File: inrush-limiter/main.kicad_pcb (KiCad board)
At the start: 2 copper layers, 27 parts, among them K1 RELAY_2RT, P1 CONN_01X04, P2 CONN_01X02, Q1 PN2222A, Q2 PN2222A, U1 LM393

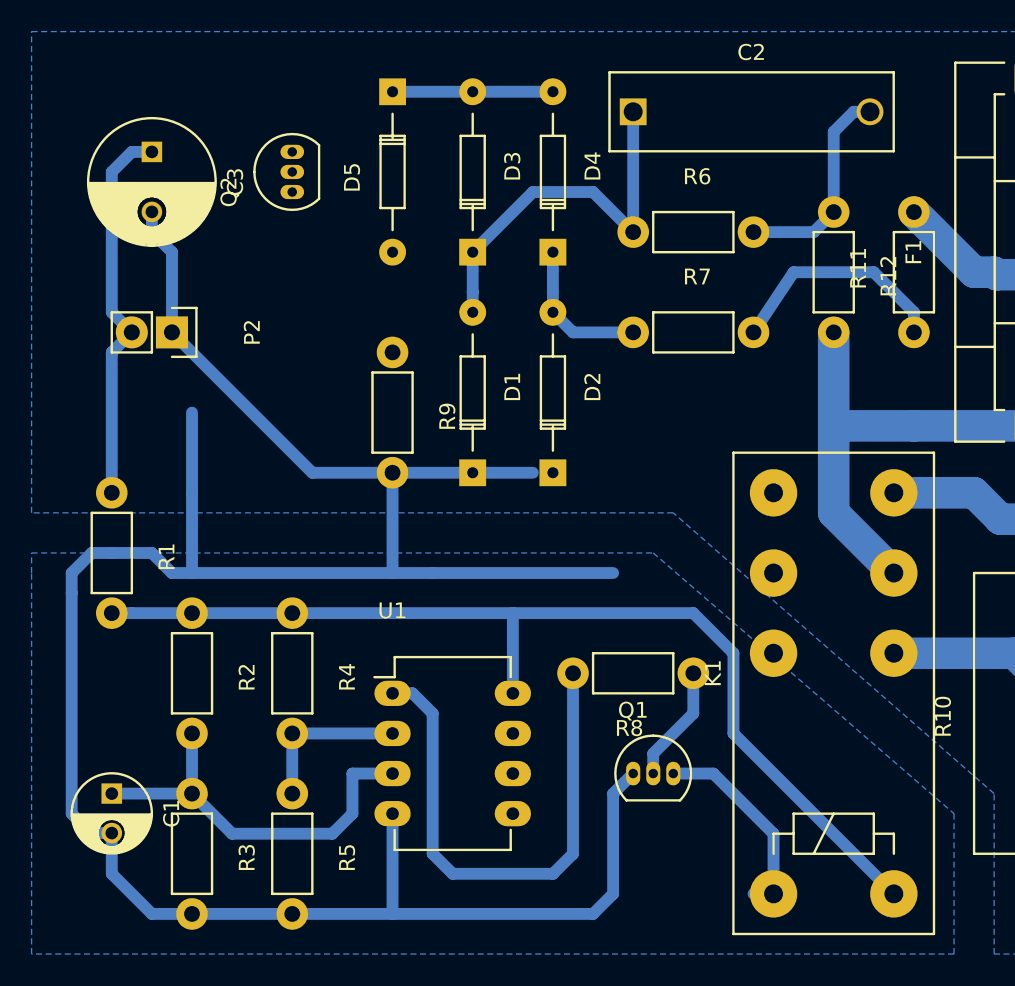
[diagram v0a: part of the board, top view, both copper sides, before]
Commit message: .25 trace and space
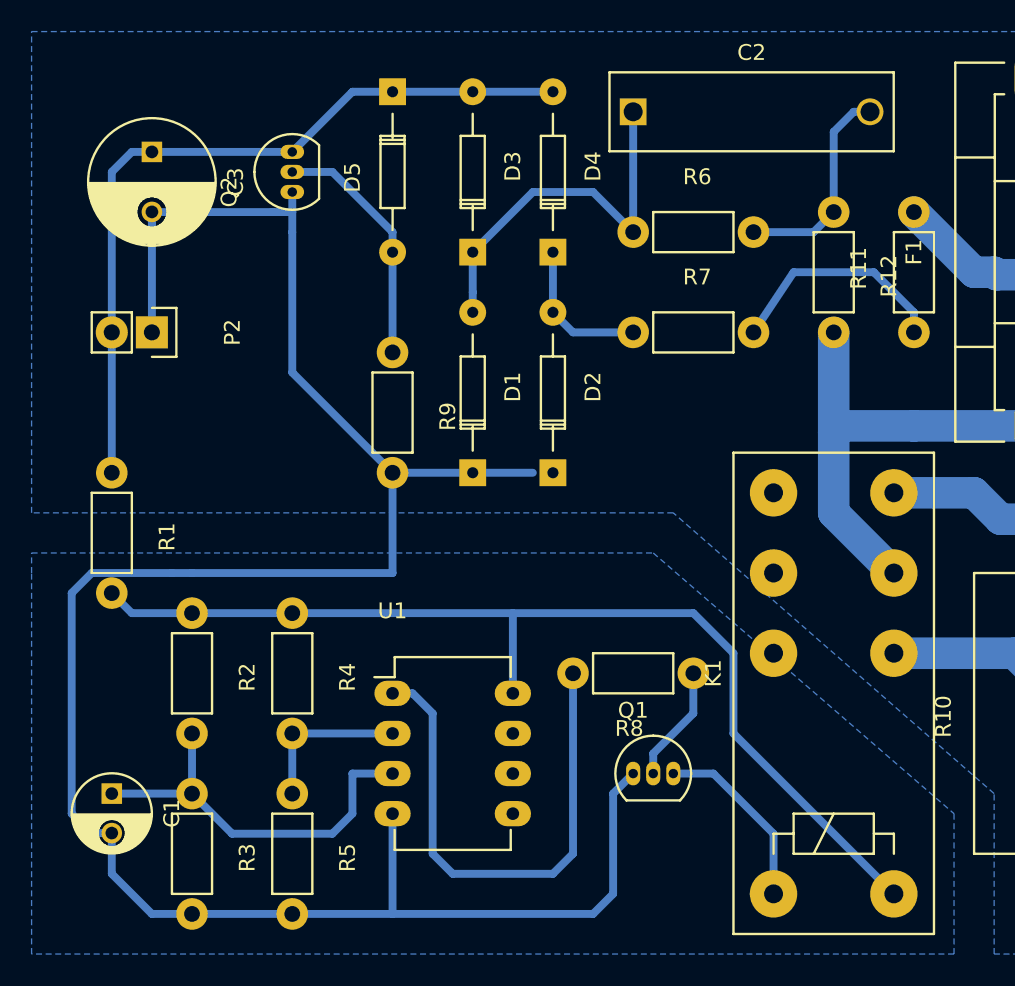
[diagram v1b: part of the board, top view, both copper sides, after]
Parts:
- moved P2 1.27 mm to (121.9, 58.4)
- moved R1 1.27 mm to (119.4, 67.3)
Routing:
- net Net-(D5-Pad2): track 0.00 -> 15.6 mm
- net +5V: track 34.6 -> 49.1 mm
- net GND: track 155.4 -> 141.9 mm
- net Net-(K1-PadA2): track 65.0 -> 65.5 mm
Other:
- net class Default: clearance 0.75 -> 0.5; trace_width 0.75 -> 0.5
- rule trace_clearance: 0.75 -> 0.5

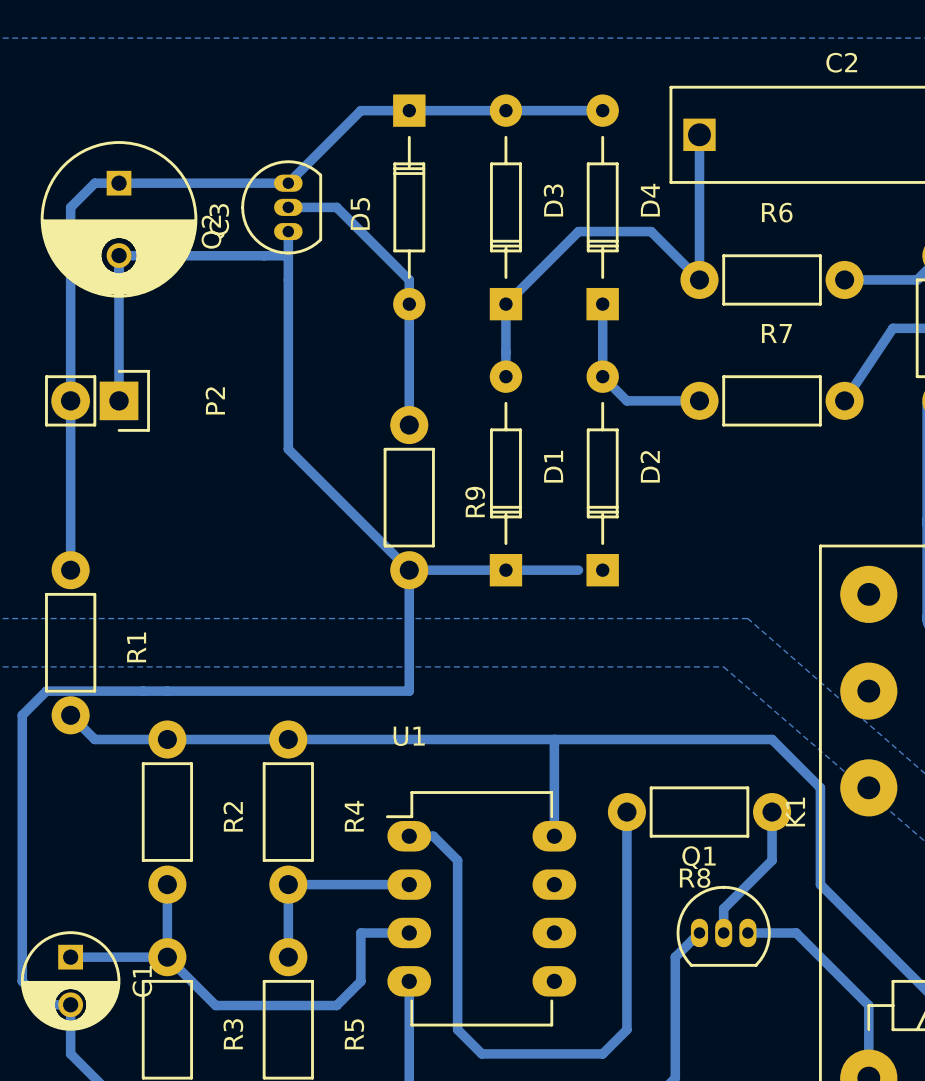
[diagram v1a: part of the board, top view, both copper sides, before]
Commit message: .5 trace and 1mm clearance
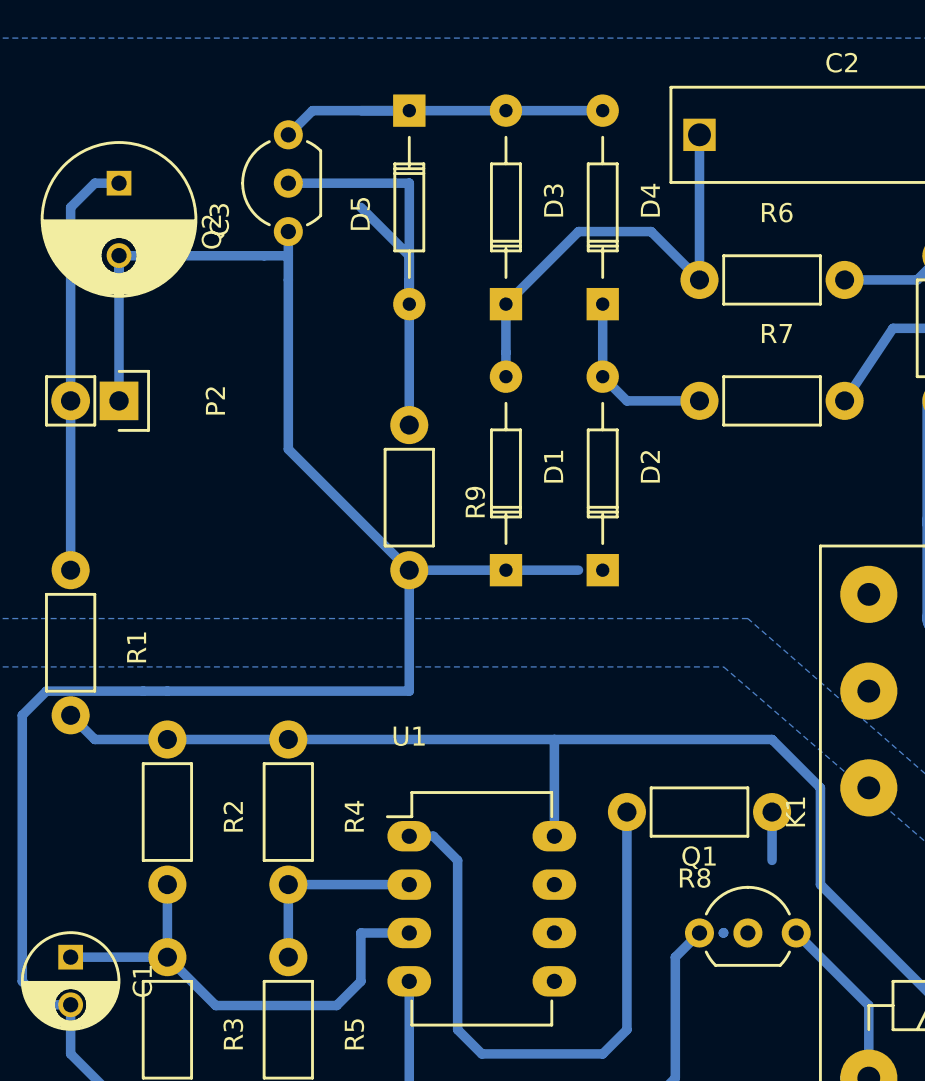
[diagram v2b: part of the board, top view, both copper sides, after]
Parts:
- Q1, Q2: footprint TO_SOT_Packages_THT:TO-92_Inline_Narrow_Oval -> TO_SOT_Packages_THT:TO-92_Inline_Wide
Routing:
- net Net-(D5-Pad2): track 15.6 -> 26.5 mm
- net +5V: track 49.1 -> 41.7 mm
- net Net-(Q1-Pad2): track 7.45 -> 2.59 mm
- net Net-(K1-PadA1): track 13.0 -> 10.5 mm
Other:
- net class Default: clearance 0.5 -> 1
- rule trace_clearance: 0.5 -> 1

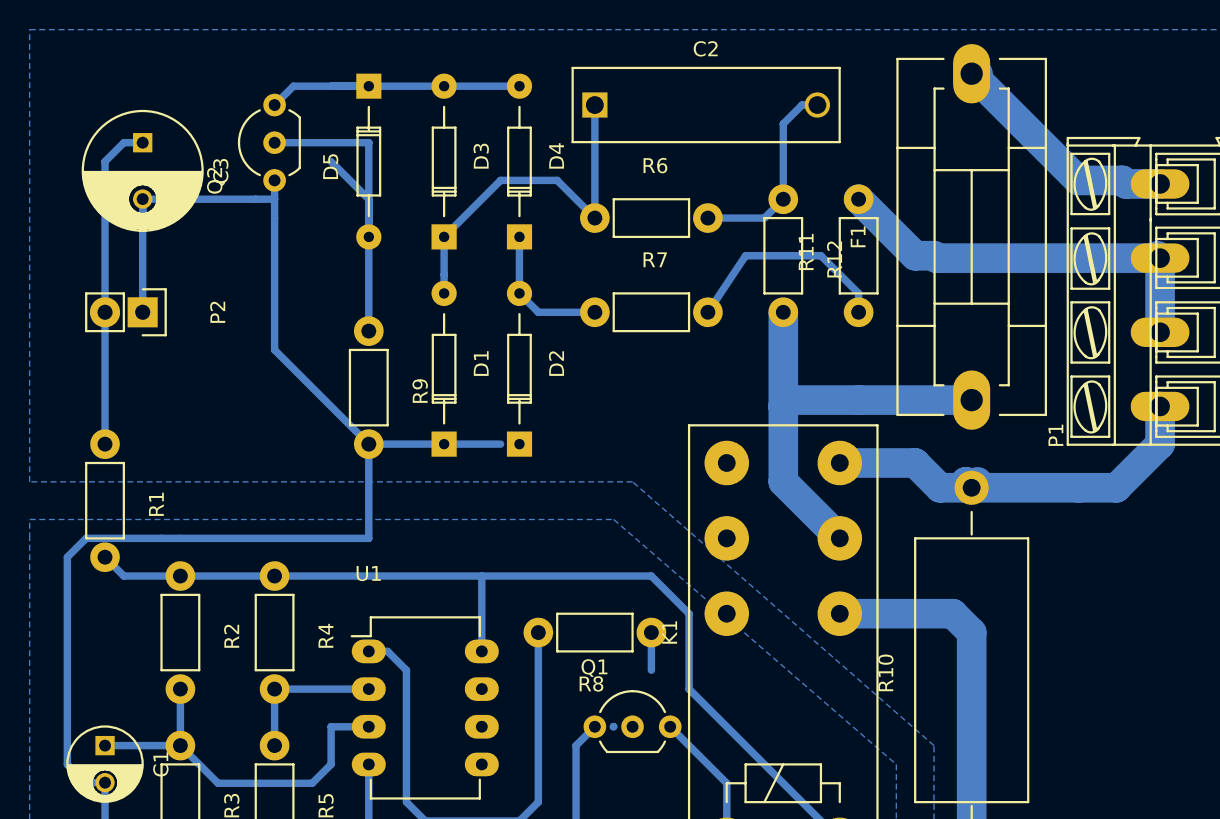
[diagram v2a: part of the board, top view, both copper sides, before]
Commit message: .5 trace and 1.25mm clearance
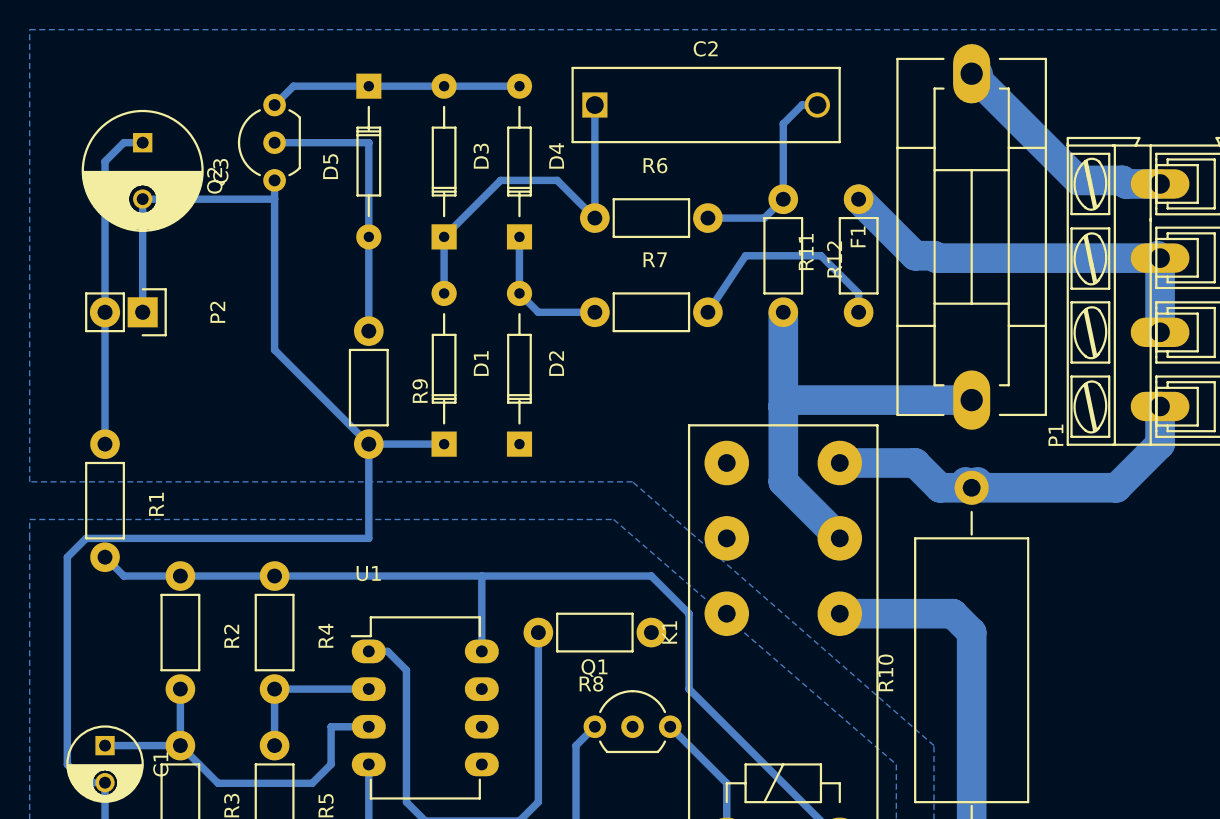
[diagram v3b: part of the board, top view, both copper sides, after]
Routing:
- net Net-(D5-Pad2): track 26.5 -> 19.1 mm
- net GND: track 141.9 -> 136.8 mm
- net Net-(Q1-Pad2): track 2.59 -> 0.00 mm
- net +5V: track 41.7 -> 39.2 mm
- net AC-live-out: track 27.7 -> 27.2 mm
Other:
- net class Default: clearance 1 -> 1.25
- rule trace_clearance: 1 -> 1.25

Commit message: update
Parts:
- moved P1 2.54 mm to (190.5, 62.2)
- moved Q2 1.27 mm to (130.8, 48.3)
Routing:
- net +5V: track 39.2 -> 48.3 mm
- net AC-live-out: track 27.2 -> 29.7 mm
- net GND: track 136.8 -> 138.0 mm
- net AC-neut: track 27.2 -> 26.1 mm
- net Net-(F1-Pad2): track 16.2 -> 15.3 mm
- net Net-(D5-Pad2): track 19.1 -> 19.6 mm
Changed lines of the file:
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@@
   (general
     (links 46)
-    (no_connects 3)
-    (area 0 0 0 0)
+    (no_connects 2)
+    (area 112.645 37.775 201.022 98.675001)
     (thickness 1.6)
     (drawings 0)
-    (tracks 124)
+    (tracks 122)
     (zones 0)
     (modules 27)
@@
   )
   (module Connect:AK300-4 (layer F.Cu)
-    (at 190.5 64.77 90)
+    (at 190.5 62.23 90)
     (descr CONNECTOR)
     (tags CONNECTOR)
@@
   )
   (module TO_SOT_Packages_THT:TO-92_Inline_Wide (layer F.Cu)
-    (at 130.81 49.53 90)
+    (at 130.81 48.26 90)
     (descr "TO-92 leads in-line, wide, drill 0.8mm (see NXP sot054_po.pdf)")
     (tags "to-92 sc-43 sc-43a sot54 PA33 transistor")
@@
   (segment (start 130.81 50.8) (end 121.93 50.8) (width 0.5) (layer B.Cu) (net 2) (status 20))
   (segment (start 130.81 60.96) (end 130.81 50.8) (width 0.5) (layer B.Cu) (net 2))
-  (segment (start 130.81 49.53) (end 130.81 50.8) (width 0.5) (layer B.Cu) (net 2) (status 10))
+  (segment (start 130.81 48.26) (end 130.81 50.8) (width 0.5) (layer B.Cu) (net 2) (status 10))
   (segment (start 137.16 67.31) (end 130.81 60.96) (width 0.5) (layer B.Cu) (net 2) (status 10))
   (segment (start 121.93 50.8) (end 121.92 50.79) (width 0.5) (layer B.Cu) (net 2) (status 30))
@@
   (segment (start 165.1 64.77) (end 165.1 69.85) (width 2) (layer B.Cu) (net 4))
   (segment (start 165.52926 64.34074) (end 165.1 64.77) (width 2) (layer B.Cu) (net 4))
+  (segment (start 121.92 46.99) (end 119.38 49.53) (width 0.5) (layer B.Cu) (net 5) (status 400000))
+  (segment (start 119.38 49.53) (end 119.38 58.42) (width 0.5) (layer B.Cu) (net 5) (status 800000))
+  (segment (start 121.92 46.99) (end 125.73 43.18) (width 0.5) (layer B.Cu) (net 5) (status 400000))
+  (segment (start 125.73 43.18) (end 130.81 43.18) (width 0.5) (layer B.Cu) (net 5) (status 800000))
   (segment (start 137.16254 43.18052) (end 132.08052 43.18052) (width 0.5) (layer B.Cu) (net 5) (status 10))
-  (segment (start 132.08052 43.18052) (end 130.81104 44.45) (width 0.5) (layer B.Cu) (net 5) (status 20))
-  (segment (start 130.81104 44.45) (end 130.81 44.45) (width 0.5) (layer B.Cu) (net 5) (status 30))
-  (segment (start 121.92 46.99) (end 120.65 46.99) (width 0.5) (layer B.Cu) (net 5) (status 10))
-  (segment (start 120.65 46.99) (end 119.38 48.26) (width 0.5) (layer B.Cu) (net 5))
-  (segment (start 119.38 48.26) (end 119.38 58.42) (width 0.5) (layer B.Cu) (net 5) (status 20))
+  (segment (start 132.08052 43.18052) (end 130.81104 43.18) (width 0.5) (layer B.Cu) (net 5) (status 20))
+  (segment (start 130.81104 43.18) (end 130.81 43.18) (width 0.5) (layer B.Cu) (net 5) (status 30))
   (segment (start 119.38 58.42) (end 119.38 67.31) (width 0.5) (layer B.Cu) (net 5) (status 30))
   (segment (start 137.16254 43.18052) (end 142.23642 43.18052) (width 0.5) (layer B.Cu) (net 5) (status 30))
@@
   (segment (start 147.31746 53.33948) (end 147.32 53.33694) (width 0.5) (layer B.Cu) (net 6) (status 30))
   (segment (start 147.32306 53.34) (end 147.32254 53.33948) (width 0.5) (layer B.Cu) (net 6) (status 30))
-  (segment (start 137.16254 53.34052) (end 137.16254 46.99254) (width 0.5) (layer B.Cu) (net 7) (status 10))
-  (segment (start 137.16 46.99) (end 130.81 46.99) (width 0.5) (layer B.Cu) (net 7) (status 20))
-  (segment (start 137.16254 46.99254) (end 137.16 46.99) (width 0.5) (layer B.Cu) (net 7))
+  (segment (start 137.16254 53.34052) (end 137.16254 46.99254) (width 0.5) (layer B.Cu) (net 7) (status 400000))
+  (segment (start 135.89 45.72) (end 130.81 45.72) (width 0.5) (layer B.Cu) (net 7) (status 800000))
+  (segment (start 137.16254 46.99254) (end 135.89 45.72) (width 0.5) (layer B.Cu) (net 7))
   (segment (start 137.16 53.33798) (end 137.16254 53.34052) (width 0.5) (layer B.Cu) (net 7) (status 30))
   (segment (start 137.16 59.69) (end 137.16 53.34306) (width 0.5) (layer B.Cu) (net 7) (status 30))
   (segment (start 137.16 53.34306) (end 137.16254 53.34052) (width 0.5) (layer B.Cu) (net 7) (status 30))
-  (segment (start 190.5 64.77) (end 190.5 67.31) (width 2) (layer B.Cu) (net 8) (status 10))
+  (segment (start 190.5 62.23) (end 190.5 67.31) (width 2) (layer B.Cu) (net 8) (status 10))
   (segment (start 187.55868 70.25132) (end 177.8 70.25132) (width 2) (layer B.Cu) (net 8) (status 20))
   (segment (start 190.5 67.31) (end 187.55868 70.25132) (width 2) (layer B.Cu) (net 8))
@@
   (segment (start 177.39868 69.85) (end 177.8 70.25132) (width 2) (layer B.Cu) (net 8) (status 30))
   (segment (start 178.20132 69.85) (end 177.8 70.25132) (width 2) (layer B.Cu) (net 8) (status 30))
-  (segment (start 190.5 59.77) (end 190.5 54.77) (width 2) (layer B.Cu) (net 9) (status 30))
-  (segment (start 170.18 50.8) (end 173.99 54.61) (width 2) (layer B.Cu) (net 9) (status 10))
-  (segment (start 175.42 54.77) (end 190.5 54.77) (width 2) (layer B.Cu) (net 9) (status 20))
-  (segment (start 175.26 54.61) (end 175.42 54.77) (width 2) (layer B.Cu) (net 9))
-  (segment (start 173.99 54.61) (end 175.26 54.61) (width 2) (layer B.Cu) (net 9))
-  (segment (start 190.5 54.77) (end 190.34 54.61) (width 2) (layer B.Cu) (net 9) (status 30))
+  (segment (start 190.5 52.23) (end 171.61 52.23) (width 2) (layer B.Cu) (net 9))
+  (segment (start 171.61 52.23) (end 170.18 50.8) (width 2) (layer B.Cu) (net 9))
+  (segment (start 190.5 57.23) (end 190.5 52.23) (width 2) (layer B.Cu) (net 9) (status 30))
+  (segment (start 190.5 52.23) (end 190.34 52.07) (width 2) (layer B.Cu) (net 9) (status 30))
   (segment (start 130.81 87.63) (end 130.81 83.82) (width 0.5) (layer B.Cu) (net 11) (status 30))
   (segment (start 130.81 83.82) (end 137.16 83.82) (width 0.5) (layer B.Cu) (net 11) (status 30))
@@
   (segment (start 160.02 52.07) (end 163.83 52.07) (width 0.5) (layer B.Cu) (net 17) (status 10))
   (segment (start 163.83 52.07) (end 164.86 51.04) (width 0.5) (layer B.Cu) (net 17) (status 20))
-  (segment (start 190.5 49.77) (end 188.2 49.77) (width 2) (layer B.Cu) (net 18) (status 10))
-  (segment (start 184.99074 49.53) (end 177.8 42.33926) (width 2) (layer B.Cu) (net 18) (status 20))
-  (segment (start 187.96 49.53) (end 184.99074 49.53) (width 2) (layer B.Cu) (net 18))
-  (segment (start 188.2 49.77) (end 187.96 49.53) (width 2) (layer B.Cu) (net 18))
+  (segment (start 190.5 47.23) (end 190.5 46.99) (width 2) (layer B.Cu) (net 18))
+  (segment (start 190.5 46.99) (end 185.84926 42.33926) (width 2) (layer B.Cu) (net 18))
+  (segment (start 185.84926 42.33926) (end 177.8 42.33926) (width 2) (layer B.Cu) (net 18))
   (segment (start 177.8 42.33926) (end 178.22926 42.33926) (width 2) (layer B.Cu) (net 18) (status 30))
   (zone (net 2) (net_name GND) (layer B.Cu) (hatch edge 0.508)
